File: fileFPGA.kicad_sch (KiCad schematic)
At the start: 11 parts, among them J2 UART, J6 JTAG, U3 LFE5U-25F-6BG256C, U6 W25Q128JVP

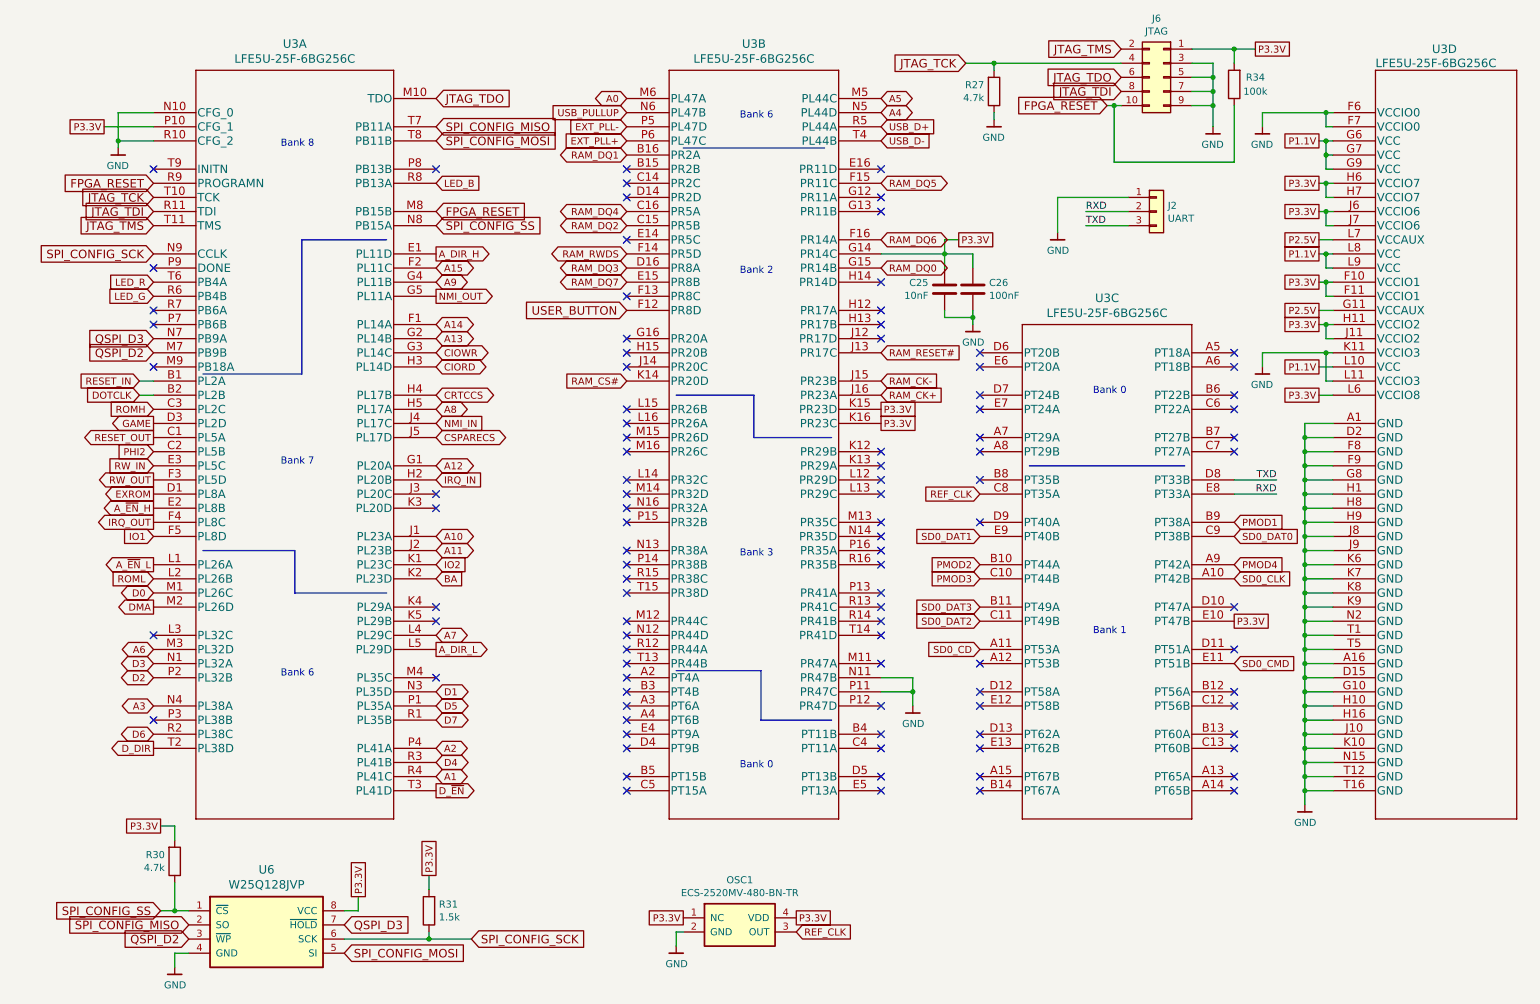
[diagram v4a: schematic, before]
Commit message: Add a dual PMOD connector with official shape
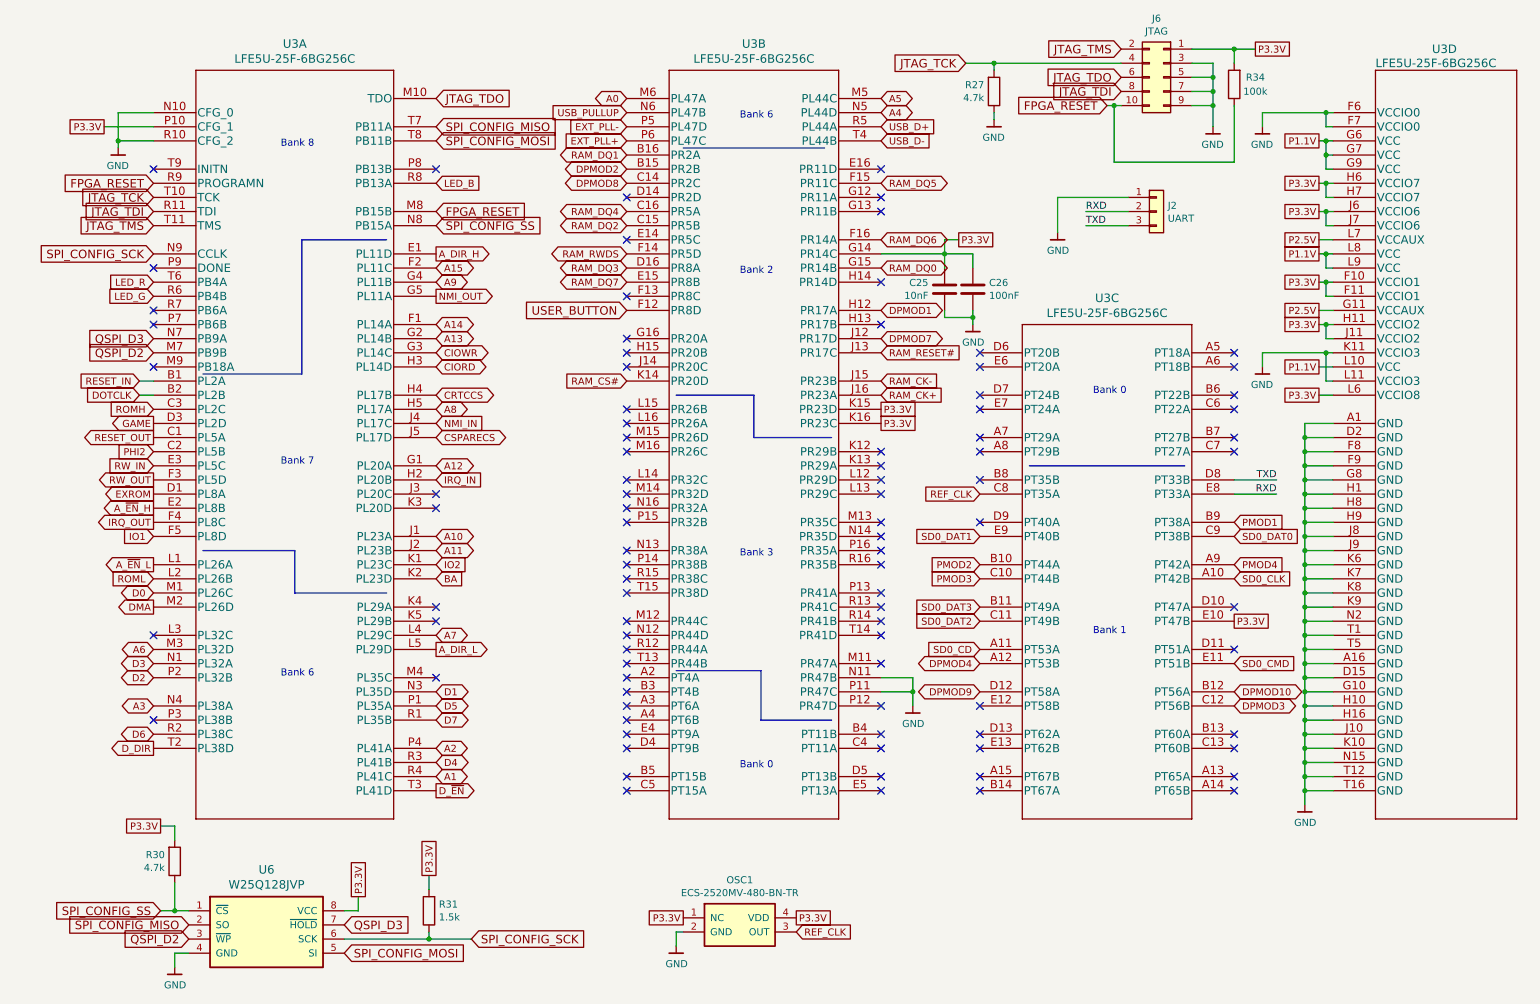
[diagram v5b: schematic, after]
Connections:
- net DPMOD2: now reaches U3.B15 (PR2B)
- net DPMOD8: now reaches U3.C14 (PR2C)
- net DPMOD1: now reaches U3.H12 (PR17A)
- net DPMOD7: now reaches U3.J12 (PR17D)
- net DPMOD4: now reaches U3.A12 (PT53B)
- net DPMOD10: now reaches U3.B12 (PT56A)
- net DPMOD3: now reaches U3.C12 (PT56B)
- net DPMOD9: now reaches U3.D12 (PT58A)
- no-connect marks 99 -> 91
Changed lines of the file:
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@@
   (no_connect (at 231.14 153.67))
   (no_connect (at 167.64 100.33))
-  (no_connect (at 231.14 140.97))
   (no_connect (at 231.14 146.05))
   (no_connect (at 231.14 130.81))
@@
   (no_connect (at 121.92 80.01))
   (no_connect (at 167.64 148.59))
-  (no_connect (at 121.92 46.99))
   (no_connect (at 121.92 100.33))
   (no_connect (at 167.64 64.77))
@@
   (no_connect (at 231.14 156.21))
   (no_connect (at 167.64 110.49))
-  (no_connect (at 167.64 69.85))
   (no_connect (at 167.64 115.57))
   (no_connect (at 121.92 148.59))
-  (no_connect (at 121.92 44.45))
   (no_connect (at 167.64 120.65))
   (no_connect (at 121.92 130.81))
@@
   (no_connect (at 167.64 123.19))
   (no_connect (at 87.63 123.19))
-  (no_connect (at 185.42 133.35))
-  (no_connect (at 167.64 74.93))
-  (no_connect (at 185.42 138.43))
   (no_connect (at 185.42 85.09))
   (no_connect (at 121.92 133.35))
@@
   (no_connect (at 167.64 140.97))
   (no_connect (at 185.42 140.97))
-  (no_connect (at 231.14 138.43))
   (no_connect (at 167.64 72.39))
   (no_connect (at 167.64 146.05))
@@
     )
   )
+  (global_label "DPMOD8" (shape bidirectional) (at 121.92 46.99 180) (fields_autoplaced)
+    (effects (font (size 1.27 1.27)) (justify right))
+    (property "Intersheet References" "${INTERSHEET_REFS}" (id 0) (at 111.7944 46.9106 0)
+      (effects (font (size 1.27 1.27)) (justify right) hide)
+    )
+  )
   (global_label "P3.3V" (shape passive) (at 167.64 87.63 0) (fields_autoplaced)
     (effects (font (size 1.27 1.27)) (justify left))
@@
     )
   )
+  (global_label "DPMOD7" (shape bidirectional) (at 167.64 74.93 0) (fields_autoplaced)
+    (effects (font (size 1.27 1.27)) (justify left))
+    (property "Intersheet References" "${INTERSHEET_REFS}" (id 0) (at 177.7656 74.8506 0)
+      (effects (font (size 1.27 1.27)) (justify left) hide)
+    )
+  )
   (global_label "SPI_CONFIG_SS" (shape input) (at 38.1 177.8 180) (fields_autoplaced)
     (effects (font (size 1.524 1.524)) (justify right))
@@
     )
   )
+  (global_label "DPMOD10" (shape bidirectional) (at 231.14 138.43 0) (fields_autoplaced)
+    (effects (font (size 1.27 1.27)) (justify left))
+    (property "Intersheet References" "${INTERSHEET_REFS}" (id 0) (at 242.4752 138.3506 0)
+      (effects (font (size 1.27 1.27)) (justify left) hide)
+    )
+  )
   (global_label "JTAG_TCK" (shape input) (at 36.83 49.53 180) (fields_autoplaced)
     (effects (font (size 1.524 1.524)) (justify right))
@@
     )
   )
+  (global_label "DPMOD1" (shape bidirectional) (at 167.64 69.85 0) (fields_autoplaced)
+    (effects (font (size 1.27 1.27)) (justify left))
+    (property "Intersheet References" "${INTERSHEET_REFS}" (id 0) (at 177.7656 69.7706 0)
+      (effects (font (size 1.27 1.27)) (justify left) hide)
+    )
+  )
   (global_label "GAME" (shape output) (at 36.83 90.17 180) (fields_autoplaced)
     (effects (font (size 1.27 1.27)) (justify right))
@@
     )
   )
+  (global_label "DPMOD4" (shape bidirectional) (at 185.42 133.35 180) (fields_autoplaced)
+    (effects (font (size 1.27 1.27)) (justify right))
+    (property "Intersheet References" "${INTERSHEET_REFS}" (id 0) (at 175.2944 133.4294 0)
+      (effects (font (size 1.27 1.27)) (justify right) hide)
+    )
+  )
   (global_label "IO1" (shape input) (at 36.83 110.49 180) (fields_autoplaced)
     (effects (font (size 1.27 1.27)) (justify right))
@@
     )
   )
+  (global_label "DPMOD9" (shape bidirectional) (at 185.42 138.43 180) (fields_autoplaced)
+    (effects (font (size 1.27 1.27)) (justify right))
+    (property "Intersheet References" "${INTERSHEET_REFS}" (id 0) (at 175.2944 138.3506 0)
+      (effects (font (size 1.27 1.27)) (justify right) hide)
+    )
+  )
   (global_label "LED_R" (shape input) (at 36.83 64.77 180) (fields_autoplaced)
     (effects (font (size 1.27 1.27)) (justify right))
@@
     )
   )
+  (global_label "DPMOD2" (shape bidirectional) (at 121.92 44.45 180) (fields_autoplaced)
+    (effects (font (size 1.27 1.27)) (justify right))
+    (property "Intersheet References" "${INTERSHEET_REFS}" (id 0) (at 111.7944 44.3706 0)
+      (effects (font (size 1.27 1.27)) (justify right) hide)
+    )
+  )
   (global_label "A_~{EN}_H" (shape output) (at 36.83 105.41 180) (fields_autoplaced)
     (effects (font (size 1.27 1.27)) (justify right))
@@
     )
   )
+  (global_label "DPMOD3" (shape bidirectional) (at 231.14 140.97 0) (fields_autoplaced)
+    (effects (font (size 1.27 1.27)) (justify left))
+    (property "Intersheet References" "${INTERSHEET_REFS}" (id 0) (at 241.2656 140.8906 0)
+      (effects (font (size 1.27 1.27)) (justify left) hide)
+    )
+  )
   (global_label "RW_OUT" (shape output) (at 36.83 100.33 180) (fields_autoplaced)
     (effects (font (size 1.27 1.27)) (justify right))
@@
   (symbol (lib_id "gkl_power:GND") (at 173.355 140.97 0) (unit 1)
     (in_bom yes) (on_board yes)
-    (property "Reference" "#PWR?" (id 0) (at 173.355 147.32 0)
+    (property "Reference" "#PWR015" (id 0) (at 173.355 147.32 0)
       (effects (font (size 1.27 1.27)) hide)
     )

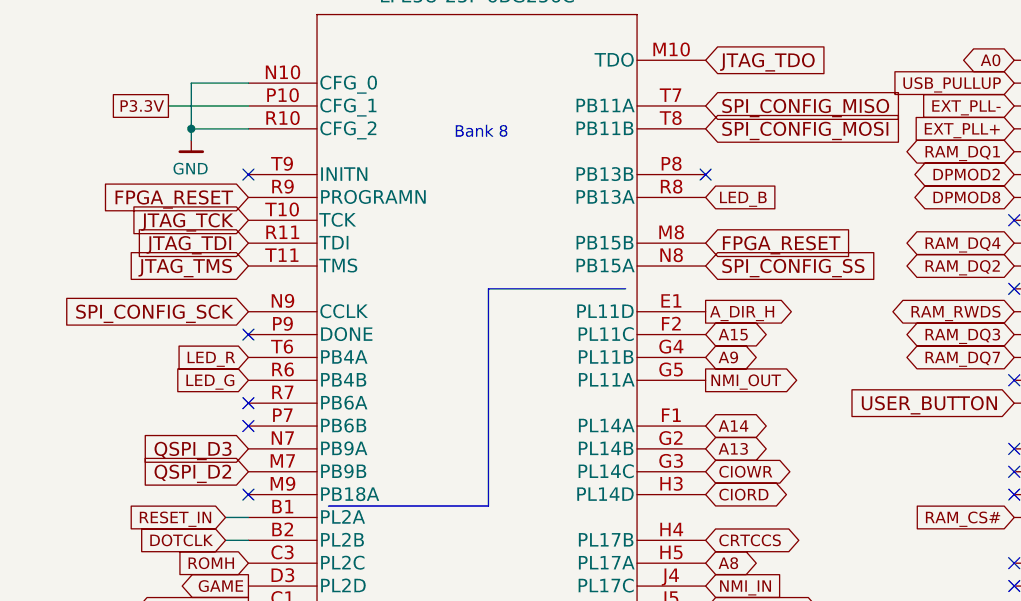
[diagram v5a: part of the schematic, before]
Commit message: Add USB-C power management chip
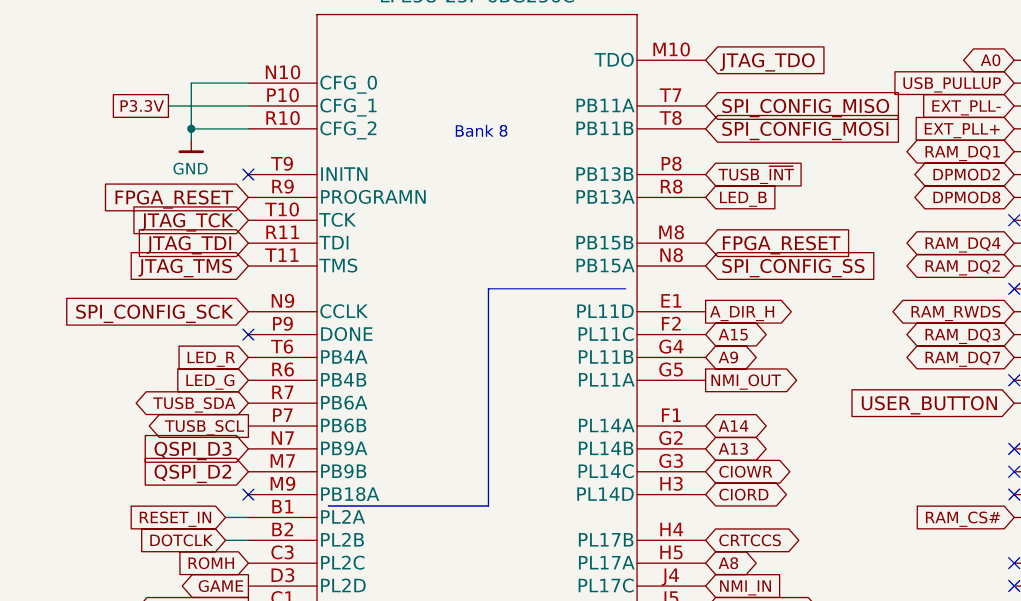
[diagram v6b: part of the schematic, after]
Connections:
- net TUSB_SCL: now reaches U3.P7 (PB6B)
- net TUSB_~{INT}: now reaches U3.P8 (PB13B)
- net TUSB_SDA: now reaches U3.R7 (PB6A)
- no-connect marks 91 -> 88
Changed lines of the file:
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@@
   (no_connect (at 167.64 95.25))
   (no_connect (at 167.64 156.21))
-  (no_connect (at 36.83 72.39))
   (no_connect (at 121.92 49.53))
   (no_connect (at 121.92 80.01))
@@
   (no_connect (at 167.64 64.77))
   (no_connect (at 121.92 102.87))
-  (no_connect (at 36.83 69.85))
   (no_connect (at 121.92 143.51))
   (no_connect (at 121.92 135.89))
@@
   (no_connect (at 167.64 120.65))
   (no_connect (at 121.92 130.81))
-  (no_connect (at 87.63 44.45))
   (no_connect (at 167.64 128.27))
   (no_connect (at 87.63 105.41))
@@
     )
   )
+  (global_label "TUSB_~{INT}" (shape input) (at 87.63 44.45 0) (fields_autoplaced)
+    (effects (font (size 1.27 1.27)) (justify left))
+    (property "Intersheet References" "${INTERSHEET_REFS}" (id 0) (at 98.6023 44.5294 0)
+      (effects (font (size 1.27 1.27)) (justify left) hide)
+    )
+  )
   (global_label "PMOD2" (shape input) (at 185.42 115.57 180) (fields_autoplaced)
     (effects (font (size 1.27 1.27)) (justify right))
@@
     )
   )
+  (global_label "TUSB_SDA" (shape bidirectional) (at 36.83 69.85 180) (fields_autoplaced)
+    (effects (font (size 1.27 1.27)) (justify right))
+    (property "Intersheet References" "${INTERSHEET_REFS}" (id 0) (at 25.1925 69.7706 0)
+      (effects (font (size 1.27 1.27)) (justify right) hide)
+    )
+  )
   (global_label "P1.1V" (shape passive) (at 246.38 39.37 180) (fields_autoplaced)
     (effects (font (size 1.27 1.27)) (justify right))
@@
     )
   )
+  (global_label "TUSB_SCL" (shape output) (at 36.83 72.39 180) (fields_autoplaced)
+    (effects (font (size 1.27 1.27)) (justify right))
+    (property "Intersheet References" "${INTERSHEET_REFS}" (id 0) (at 25.2529 72.3106 0)
+      (effects (font (size 1.27 1.27)) (justify right) hide)
+    )
+  )

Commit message: Update component prices
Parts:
- C25: Pricing (EUR) 0,09 -> 0,08
- J2: Pricing (EUR) 0,32 -> 0,68
- J6: Pricing (EUR) 3,02 -> 2,86
- OSC1: Pricing (EUR) 1,23 -> 0,97
- R27, R30: Pricing (EUR) 0,10 -> 0,09
- R31, R34: Pricing (EUR) 0,11 -> 0,09
- U6: Pricing (EUR) 1,94 -> 1,63
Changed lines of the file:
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@@
       (effects (font (size 1.27 1.27)) hide)
     )
-    (property "Pricing (EUR)" "3,02" (at 218.44 27.94 0)
+    (property "Pricing (EUR)" "2,86" (at 218.44 27.94 0)
       (effects (font (size 1.27 1.27)) hide)
     )
@@
       (effects (font (size 1.27 1.27)) hide)
     )
-    (property "Pricing (EUR)" "0,10" (at 187.96 30.48 0)
+    (property "Pricing (EUR)" "0,09" (at 187.96 30.48 0)
       (effects (font (size 1.27 1.27)) hide)
     )
@@
       (effects (font (size 1.27 1.27)) hide)
     )
-    (property "Pricing (EUR)" "1,94" (at 57.15 181.61 0)
+    (property "Pricing (EUR)" "1,63" (at 57.15 181.61 0)
       (effects (font (size 1.27 1.27)) hide)
     )
@@
       (effects (font (size 1.27 1.27)) hide)
     )
-    (property "Pricing (EUR)" "1,23" (at 142.24 180.34 0)
+    (property "Pricing (EUR)" "0,97" (at 142.24 180.34 0)
       (effects (font (size 1.27 1.27)) hide)
     )
@@
       (effects (font (size 1.27 1.27)) hide)
     )
-    (property "Pricing (EUR)" "0,09" (at 179.07 66.04 0)
+    (property "Pricing (EUR)" "0,08" (at 179.07 66.04 0)
       (effects (font (size 1.27 1.27)) hide)
     )
@@
       (effects (font (size 1.27 1.27)) hide)
     )
-    (property "Pricing (EUR)" "0,11" (at 86.36 177.8 0)
+    (property "Pricing (EUR)" "0,09" (at 86.36 177.8 0)
       (effects (font (size 1.27 1.27)) hide)
     )
@@
       (effects (font (size 1.27 1.27)) hide)
     )
-    (property "Pricing (EUR)" "0,10" (at 40.64 168.91 0)
+    (property "Pricing (EUR)" "0,09" (at 40.64 168.91 0)
       (effects (font (size 1.27 1.27)) hide)
     )
@@
       (effects (font (size 1.27 1.27)) hide)
     )
-    (property "Pricing (EUR)" "0,32" (at 217.17 52.07 0)
+    (property "Pricing (EUR)" "0,68" (at 217.17 52.07 0)
       (effects (font (size 1.27 1.27)) hide)
     )
@@
       (effects (font (size 1.27 1.27)) hide)
     )
-    (property "Pricing (EUR)" "0,11" (at 231.14 29.21 0)
-      (effects (font (size 1.27 1.27)) hide)
-    )
+    (property "Pricing (EUR)" "0,09" (at 231.14 29.21 0)
+      (effects (font (size 1.27 1.27)) hide)
+    )
